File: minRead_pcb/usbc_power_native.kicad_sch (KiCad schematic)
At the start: 18 parts, among them J1 USB_C_Receptacle, U2 BQ24074RGT, U3 AP2112K-3.3

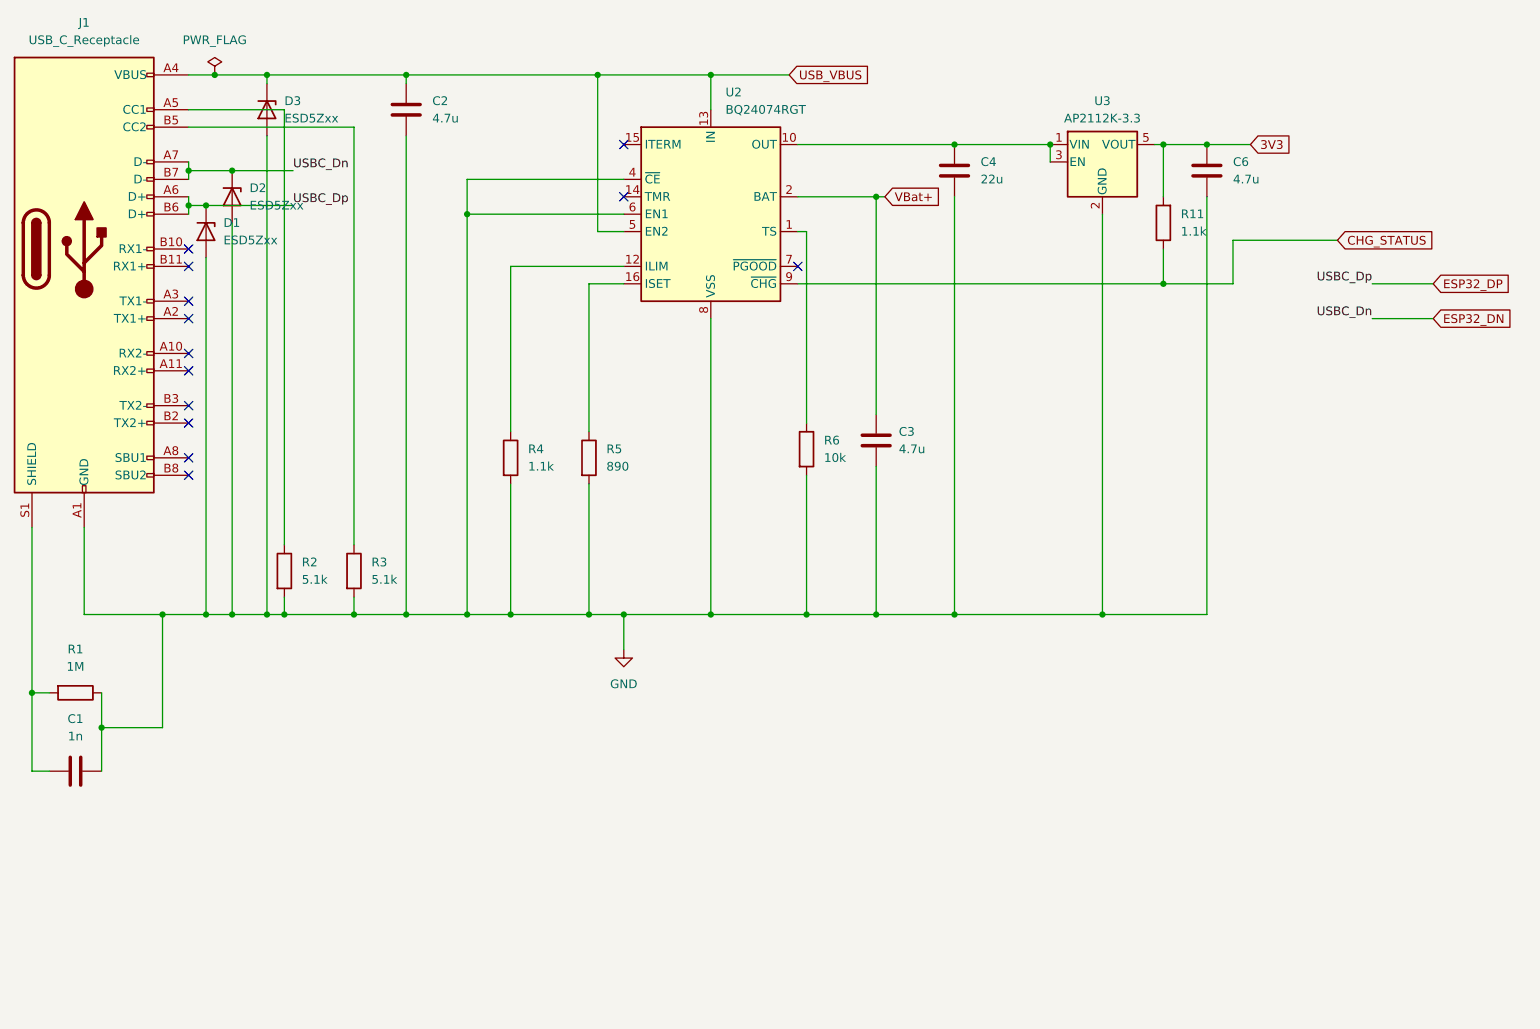
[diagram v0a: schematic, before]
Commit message: - schematic updates: - usb500 mode enabled on bq - charge limit set to 100mA 8.9kohm (safe for small batteries) - series resistors on sd card and epd lines - esd arrays for usb-c and sd-card - increased output cap for ldo from 4.7u to 22u - added pgood to gpio - confirmed reverse polarity stuff - cap to ground instead of series for sd card vdd - fixed cap values on epd
new layout:
- adjusted board size
- very compact
- need to fill ground planes and check drc errors (a lot because of solder mask)
- need to adjust jst footprint in case there's a better choice
- review review review
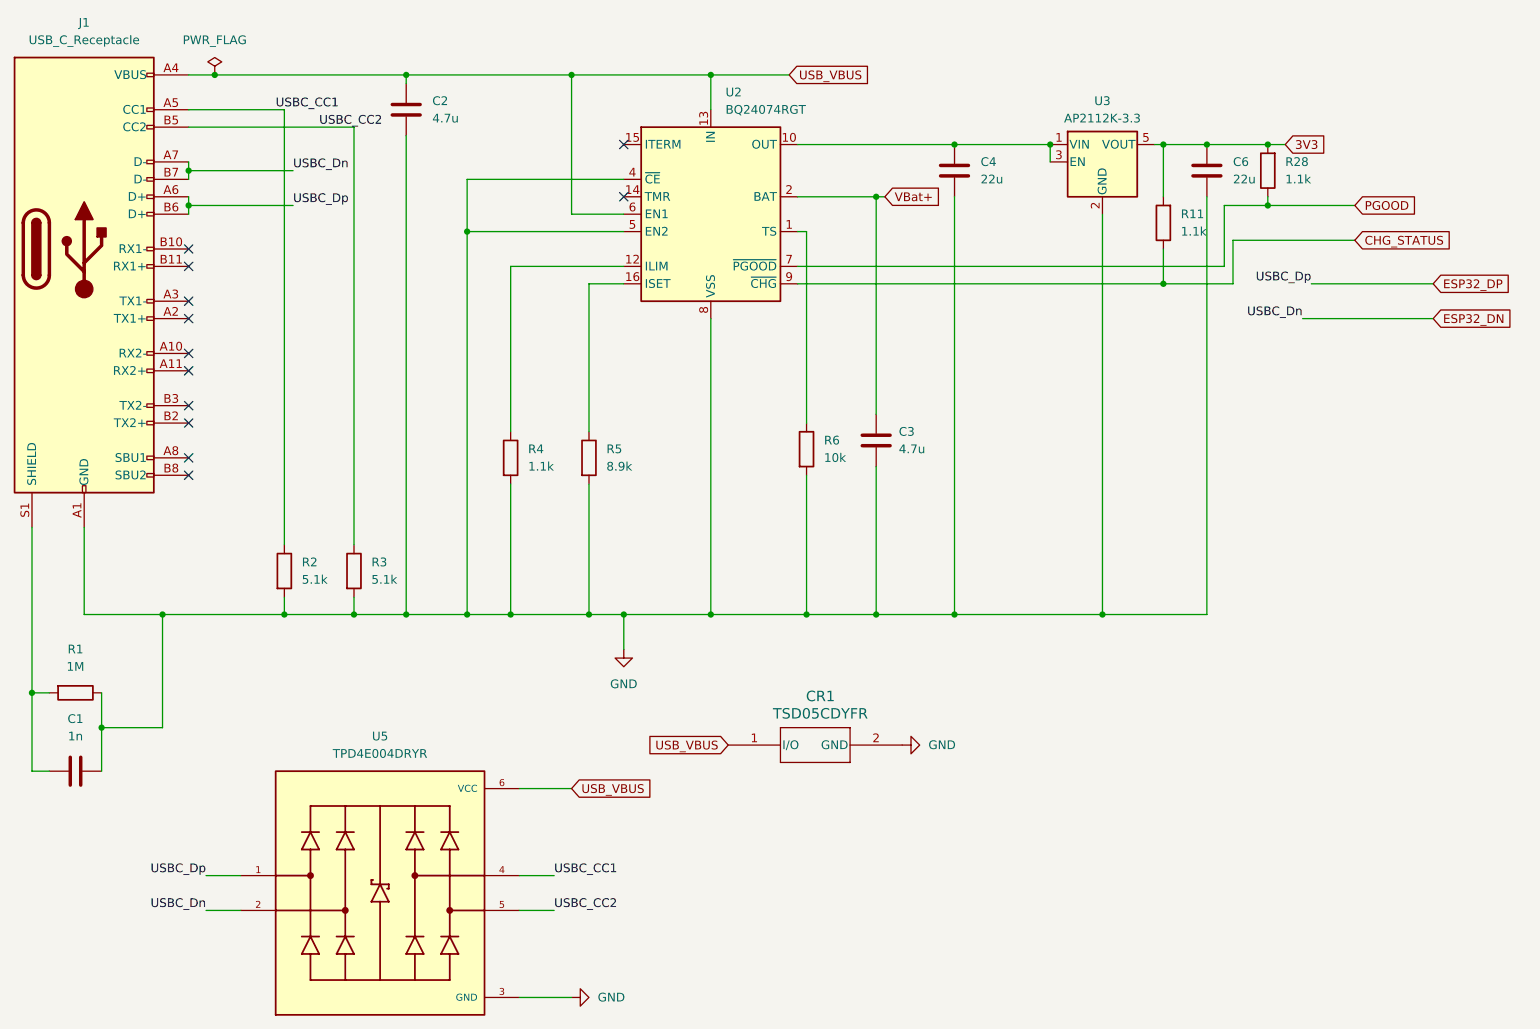
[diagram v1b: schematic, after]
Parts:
- removed D1, D2, D3: ESD5Zxx, Diode_SMD:D_SOD-523, symbol Diode:ESD5Zxx
- added CR1: TSD05CDYFR, footprints:TVS_SOD2_DYF_TEX-M, symbol TSD05CDYFR:TSD05CDYFR
- added R28: 1.1k, Resistor_SMD:R_0805_2012Metric_Pad1.20x1.40mm_HandSolder, symbol Device:R
- added U5: TPD4E004DRYR, TPD4E004DRYR:PSON50P145X100X60-6N, symbol TPD4E004DRYR:TPD4E004DRYR
- C6: value 4.7u -> 22u
- R5: value 890 -> 8.9k
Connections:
- net 3V3: now also R28.2
- net ESP32_DN: now also U5.2
- net ESP32_DP: now also U5.1
- net GND: now also U2.5 (EN2), CR1.2 (GND), U5.3 (GND); no longer U2.6 (EN1)
- net USB_VBUS: now also U2.6 (EN1), CR1.1 (I/O), U5.6 (VCC); no longer U2.5 (EN2)
- net USBC_CC1: now reaches J1.A5 (CC1), R2.1
- net USBC_CC1: now also U5.4
- net PGOOD: now reaches U2.7 (~{PGOOD})
- net PGOOD: now also R28.1
- net USBC_CC2: now reaches J1.B5 (CC2), R3.1
- net USBC_CC2: now also U5.5
- no-connect marks 13 -> 12

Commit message: - fixed diode orientation of eink booster - everything works except eink driver: - rst pin pulls high, dc doesn't toggle, etc etc. - TODO for next rev: - remove reset stabilizer and just route 3v3 to epd inductor circuit - replace esd arrays with hand-solderable components (qfn to sot) - replace buttons with resistor ladder circuit (xteink-like) - replace bq24074 with more discrete charging circuit to aid hand-solder - add led driver (15v to 7 series LEDs) - replace usb-c receptacle with through-hole - add external dupont pins for external LED driver access and spare GPIOs
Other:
- moved on the sheet: C4
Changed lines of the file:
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@@
+	)
+	(junction
+		(at 198.12 66.04)
+		(diameter 0)
+		(color 0 0 0 0)
 	)
 	(junction
@@
 	)
 	(junction
+		(at 198.12 134.62)
+		(diameter 0)
+		(color 0 0 0 0)
+	)
+	(junction
 		(at 67.31 151.13)
 		(diameter 0)
@@
 	)
 	(junction
-		(at 191.77 66.04)
-		(diameter 0)
-		(color 0 0 0 0)
-	)
-	(junction
 		(at 104.14 134.62)
-		(diameter 0)
-		(color 0 0 0 0)
-	)
-	(junction
-		(at 191.77 134.62)
 		(diameter 0)
 		(color 0 0 0 0)
@@
 	(wire
 		(pts
-			(xy 191.77 73.66) (xy 191.77 134.62)
+			(xy 198.12 73.66) (xy 198.12 134.62)
 		)
 		(stroke
@@
 	(wire
 		(pts
-			(xy 180.34 134.62) (xy 191.77 134.62)
+			(xy 180.34 134.62) (xy 198.12 134.62)
 		)
 		(stroke
@@
 	(wire
 		(pts
+			(xy 198.12 66.04) (xy 205.74 66.04)
+		)
+		(stroke
+			(width 0)
+			(type default)
+		)
+	)
+	(wire
+		(pts
 			(xy 143.51 139.7) (xy 143.51 134.62)
 		)
@@
 	(wire
 		(pts
-			(xy 213.36 134.62) (xy 191.77 134.62)
+			(xy 213.36 134.62) (xy 198.12 134.62)
 		)
 		(stroke
@@
 	(wire
 		(pts
-			(xy 168.91 66.04) (xy 191.77 66.04)
+			(xy 168.91 66.04) (xy 198.12 66.04)
 		)
 		(stroke
@@
 		(pts
 			(xy 80.01 68.58) (xy 80.01 69.85)
-		)
-		(stroke
-			(width 0)
-			(type default)
-		)
-	)
-	(wire
-		(pts
-			(xy 191.77 66.04) (xy 205.74 66.04)
 		)
 		(stroke
@@
 	(symbol
 		(lib_id "Device:C")
-		(at 191.77 69.85 0)
+		(at 198.12 69.85 0)
 		(unit 1)
 		(exclude_from_sim no)
@@
 		(fields_autoplaced yes)
 		(property "Reference" "C4"
-			(at 195.58 68.5799 0)
+			(at 201.93 68.5799 0)
 			(effects
 				(font
@@
 		)
 		(property "Value" "22u"
-			(at 195.58 71.1199 0)
+			(at 201.93 71.1199 0)
 			(effects
 				(font
@@
 		)
 		(property "Footprint" "Capacitor_SMD:C_0805_2012Metric_Pad1.18x1.45mm_HandSolder"
-			(at 192.7352 73.66 0)
+			(at 199.0852 73.66 0)
 			(effects
 				(font
@@
 		)
 		(property "Datasheet" "~"
-			(at 191.77 69.85 0)
+			(at 198.12 69.85 0)
 			(effects
 				(font
@@
 		)
 		(property "Description" "Unpolarized capacitor"
-			(at 191.77 69.85 0)
-			(effects
-				(font
+			(at 198.12 69.85 0)
+			(effects
+				(font

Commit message: gigantic commit, my bad revised schematic to sanity check turns out my fpc was flipped, now fixed added following schematics: - battery protection circuit - series LED driver - external peripheral connector for unused GPIO revised following schematics: - power path, replaced with mcp charger and FET rather than bq - buttons, opted for resistor ladder circuit, added two more for xte compatibility - eink driver, opted to change to updated components from waveshare 2.3 - updated esd components for usb-c and sdmmc - updated usb-c receptacle, now through-hole
New layout:
- mostly same as last time, but work done to ensure good grounding for LED/eink circuits
- eink gpio has minimal crossing/coupling just in case
- esp32 and 24 pin headers have longer pads hopefully for easier soldering
- external header in corner back of device
- prettier passive component layout
- fat 3v3 traces and small zone fill

- todo:
- DRC errors, mostly clearance and silkscreen overlap
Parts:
- removed C1: 1n, Capacitor_SMD:C_0805_2012Metric_Pad1.18x1.45mm_HandSolder, symbol Device:C
- removed C2, C3: 4.7u, Capacitor_SMD:C_0805_2012Metric_Pad1.18x1.45mm_HandSolder, symbol Device:C
- removed C4, C6: 22u, Capacitor_SMD:C_0805_2012Metric_Pad1.18x1.45mm_HandSolder, symbol Device:C
- removed CR1: TSD05CDYFR, footprints:TVS_SOD2_DYF_TEX-M, symbol TSD05CDYFR:TSD05CDYFR
- removed J1: USB_C_Receptacle, Connector_USB:USB_C_Receptacle_Amphenol_12401610E4-2A, symbol Connector:USB_C_Receptacle
- removed R1: 1M, Resistor_SMD:R_0805_2012Metric_Pad1.20x1.40mm_HandSolder, symbol Device:R
- removed R11, R28, R4: 1.1k, Resistor_SMD:R_0805_2012Metric_Pad1.20x1.40mm_HandSolder, symbol Device:R
- removed R2, R3: 5.1k, Resistor_SMD:R_0805_2012Metric_Pad1.20x1.40mm_HandSolder, symbol Device:R
- removed R5: 8.9k, Resistor_SMD:R_0805_2012Metric_Pad1.20x1.40mm_HandSolder, symbol Device:R
- removed R6: 10k, Resistor_SMD:R_0805_2012Metric_Pad1.20x1.40mm_HandSolder, symbol Device:R
- removed U2: BQ24074RGT, Package_DFN_QFN:VQFN-16-1EP_3x3mm_P0.5mm_EP1.6x1.6mm, symbol Battery_Management:BQ24074RGT
- removed U3: AP2112K-3.3, Package_TO_SOT_SMD:SOT-23-5_HandSoldering, symbol Regulator_Linear:AP2112K-3.3
- removed U5: TPD4E004DRYR, TPD4E004DRYR:PSON50P145X100X60-6N, symbol TPD4E004DRYR:TPD4E004DRYR
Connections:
- no-connect marks 12 -> 0
